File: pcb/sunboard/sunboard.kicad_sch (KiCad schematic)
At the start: 198 parts, among them SW1 SW_Push_LED, SW10 SW_Push_LED, SW100 SW_Push_LED, SW101 SW_Push_LED, SW102 SW_Push_LED, SW103 SW_Push_LED, SW104 SW_Push_LED, SW105 SW_Push_LED, SW106 SW_Push_LED, SW107 SW_Push_LED, SW108 SW_Push_LED, SW109 SW_Push_LED, SW11 SW_Push_LED, SW110 SW_Push_LED, SW111 SW_Push_LED, SW112 SW_Push_LED, SW113 SW_Push_LED, SW114 SW_Push_LED, SW115 SW_Push_LED, SW116 SW_Push_LED, SW117 SW_Push_LED, SW118 SW_Push_LED, SW119 SW_Push_LED, SW12 SW_Push_LED, SW120 SW_Push_LED, SW121 SW_Push_LED, SW122 SW_Push_LED, SW123 SW_Push_LED, SW124 SW_Push_LED, SW125 SW_Push_LED, SW126 SW_Push_LED, SW127 SW_Push_LED, SW128 SW_Push_LED, SW129 SW_Push_LED, SW13 SW_Push_LED, SW130 SW_Push_LED, SW131 SW_Push_LED, SW132 SW_Push_LED, SW133 SW_Push_LED, SW134 SW_Push_LED, SW135 SW_Push_LED, SW136 SW_Push_LED, SW137 SW_Push_LED, SW138 SW_Push_LED, SW139 SW_Push_LED, SW14 SW_Push_LED, SW140 SW_Push_LED, SW141 SW_Push_LED, SW142 SW_Push_LED, SW143 SW_Push_LED, SW144 SW_Push_LED, SW145 SW_Push_LED, SW146 SW_Push_LED, SW147 SW_Push_LED, SW148 SW_Push_LED, SW149 SW_Push_LED, SW15 SW_Push_LED, SW150 SW_Push_LED, SW151 SW_Push_LED, SW152 SW_Push_LED, SW153 SW_Push_LED, SW154 SW_Push_LED, SW155 SW_Push_LED, SW156 SW_Push_LED, SW157 SW_Push_LED, SW158 SW_Push_LED, SW159 SW_Push_LED, SW16 SW_Push_LED, SW160 SW_Push_LED, SW161 SW_Push_LED, SW162 SW_Push_LED, SW163 SW_Push_LED, SW164 SW_Push_LED, SW165 SW_Push_LED, SW166 SW_Push_LED, SW167 SW_Push_LED, SW168 SW_Push_LED, SW169 SW_Push_LED, SW17 SW_Push_LED, SW170 SW_Push_LED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

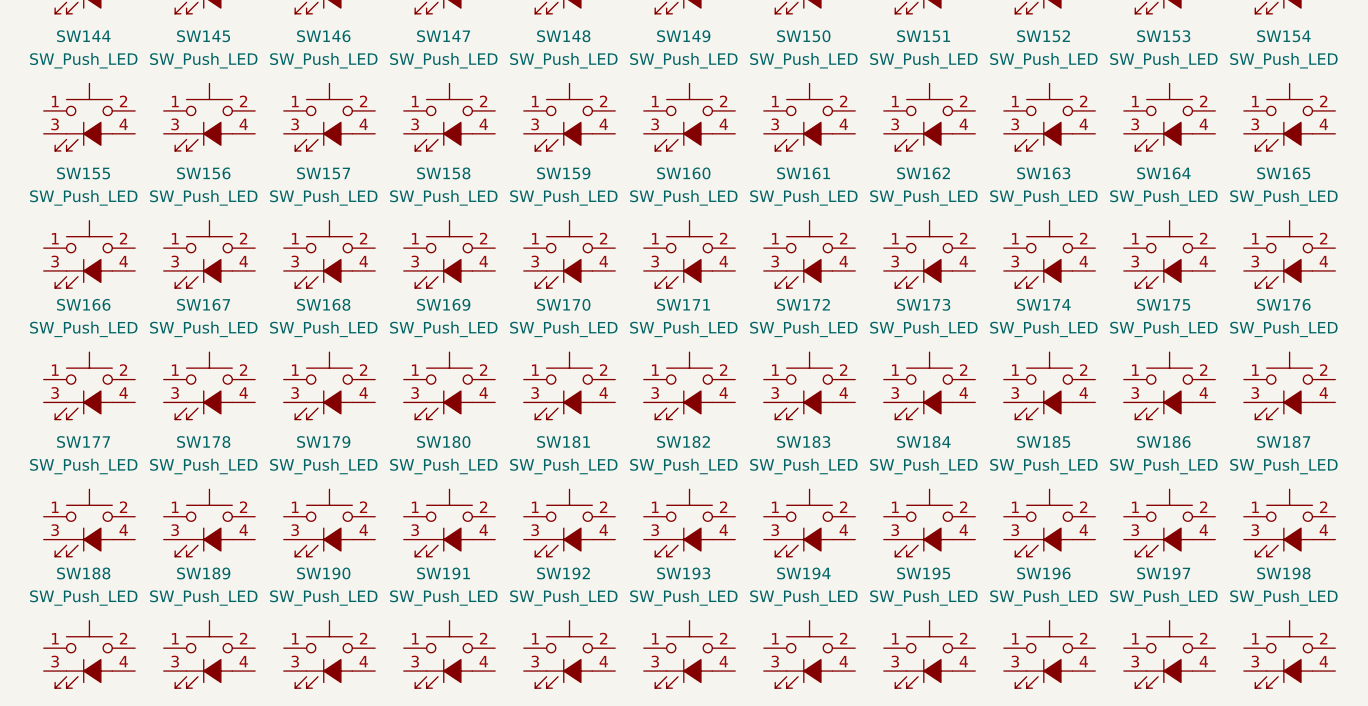
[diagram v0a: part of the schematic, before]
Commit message: feat: remove bottom 4 rows of buttons (footholds)
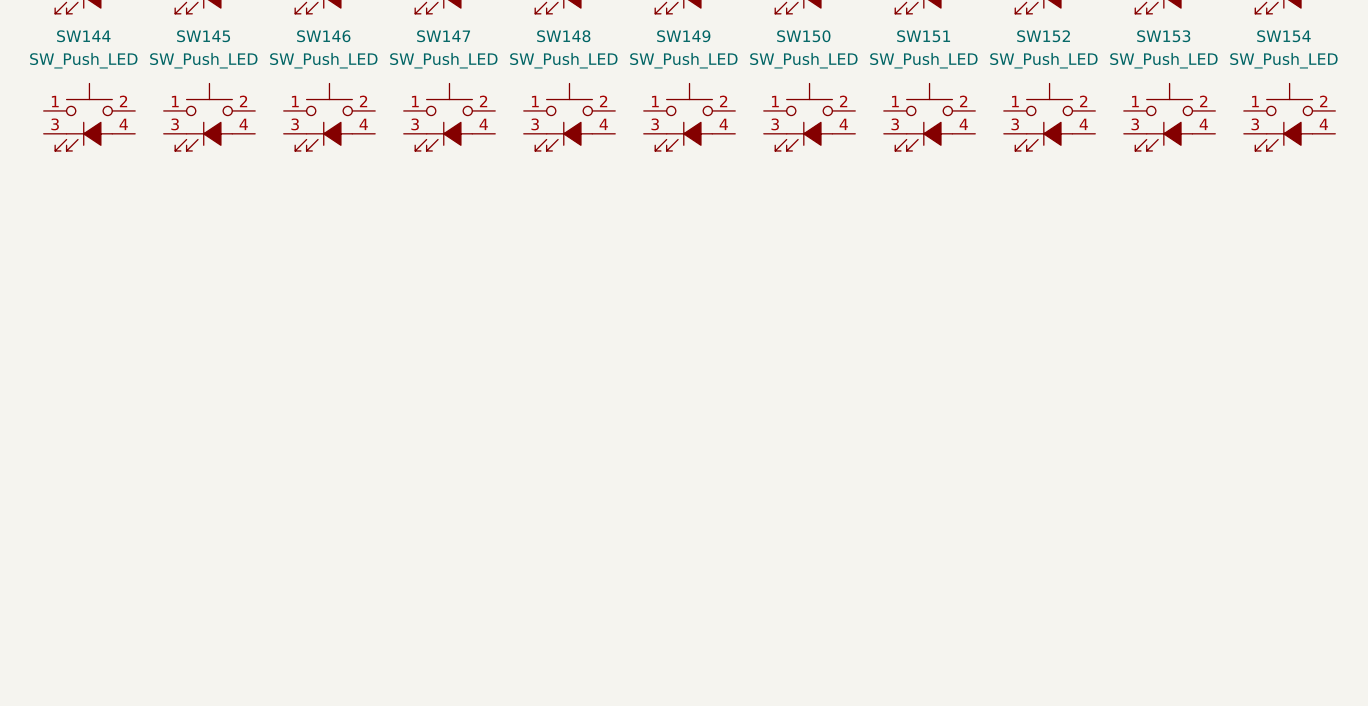
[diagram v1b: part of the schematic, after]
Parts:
- removed SW155, SW156, SW157, SW158, SW159, SW160, SW161, SW162, SW163, SW164, SW165, SW166, SW167, SW168, SW169, SW170, SW171, SW172, SW173, SW174, SW175, SW176, SW177, SW178, SW179, SW180, SW181, SW182, SW183, SW184, SW185, SW186, SW187, SW188, SW189, SW190, SW191, SW192, SW193, SW194, SW195, SW196, SW197, SW198: SW_Push_LED, symbol Switch:SW_Push_LED

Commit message: feat: get basic POC for 8x8 out
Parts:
- removed SW10, SW100, SW101, SW102, SW103, SW104, SW105, SW106, SW107, SW108, SW109, SW11, SW110, SW111, SW112, SW113, SW114, SW115, SW116, SW117, SW118, SW119, SW120, SW121, SW122, SW123, SW124, SW125, SW126, SW127, SW128, SW129, SW130, SW131, SW132, SW133, SW134, SW135, SW136, SW137, SW138, SW139, SW140, SW141, SW142, SW143, SW144, SW145, SW146, SW147, SW148, SW149, SW150, SW151, SW152, SW153, SW154, SW20, SW21, SW22, SW31, SW32, SW33, SW42, SW43, SW44, SW53, SW54, SW55, SW64, SW65, SW66, SW75, SW76, SW77, SW86, SW87, SW88, SW89, SW9, SW90, SW91, SW92, SW93, SW94, SW95, SW96, SW97, SW98, SW99: SW_Push_LED, symbol Switch:SW_Push_LED
- added A?: Adafruit_Feather_HUZZAH32_ESP32, Module:Adafruit_Feather, symbol MCU_Module:Adafruit_Feather_HUZZAH32_ESP32
- added U?: 74LS148, symbol 74xx:74LS148
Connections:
- net at SW74.2: now also SW19.2, SW19.4 (A), SW30.2, SW30.4 (A), SW41.2, SW41.4 (A), SW52.2, SW52.4 (A), SW63.2, SW63.4 (A), SW74.4 (A), SW8.2, SW8.4 (A), SW85.2, U?.11 (I1)
- net at SW70.2: now also SW15.2, SW15.4 (A), SW26.2, SW26.4 (A), SW37.2, SW37.4 (A), SW4.2, SW4.4 (A), SW48.2, SW48.4 (A), SW59.2, SW59.4 (A), SW70.4 (A), SW81.2, U?.2 (I5)
- net at SW72.2: now also SW17.2, SW17.4 (A), SW28.2, SW28.4 (A), SW39.2, SW39.4 (A), SW50.2, SW50.4 (A), SW6.2, SW6.4 (A), SW61.2, SW61.4 (A), SW72.4 (A), SW83.2, U?.13 (I3)
- net at SW24.2: now also SW13.2, SW13.4 (A), SW2.2, SW2.4 (A), SW24.4 (A), SW35.2, SW35.4 (A), SW46.2, SW46.4 (A), SW57.2, SW57.4 (A), SW68.2, SW68.4 (A), SW79.2, U?.4 (I7)
- net at SW45.2: now also SW1.2, SW1.4 (A), SW12.2, SW23.2, SW23.4 (A), SW34.2, SW34.4 (A), SW45.4 (A), SW56.2, SW56.4 (A), SW67.2, SW67.4 (A), SW78.2, U?.5 (EI)
- net at SW62.2: now also SW18.2, SW18.4 (A), SW29.2, SW29.4 (A), SW40.2, SW40.4 (A), SW51.2, SW51.4 (A), SW62.4 (A), SW7.2, SW7.4 (A), SW73.2, SW73.4 (A), SW84.2, U?.12 (I2)
- net at SW25.2: now also SW14.2, SW14.4 (A), SW25.4 (A), SW3.2, SW3.4 (A), SW36.2, SW36.4 (A), SW47.2, SW47.4 (A), SW58.2, SW58.4 (A), SW69.2, SW69.4 (A), SW80.2, U?.3 (I6)
- net at SW60.2: now also SW16.2, SW16.4 (A), SW27.2, SW27.4 (A), SW38.2, SW38.4 (A), SW49.2, SW49.4 (A), SW5.2, SW5.4 (A), SW60.4 (A), SW71.2, SW71.4 (A), SW82.2, U?.1 (I4)
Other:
- moved on the sheet: SW1, SW12, SW13, SW14, SW15, SW16, SW17, SW18, SW19, SW2, SW23, SW24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

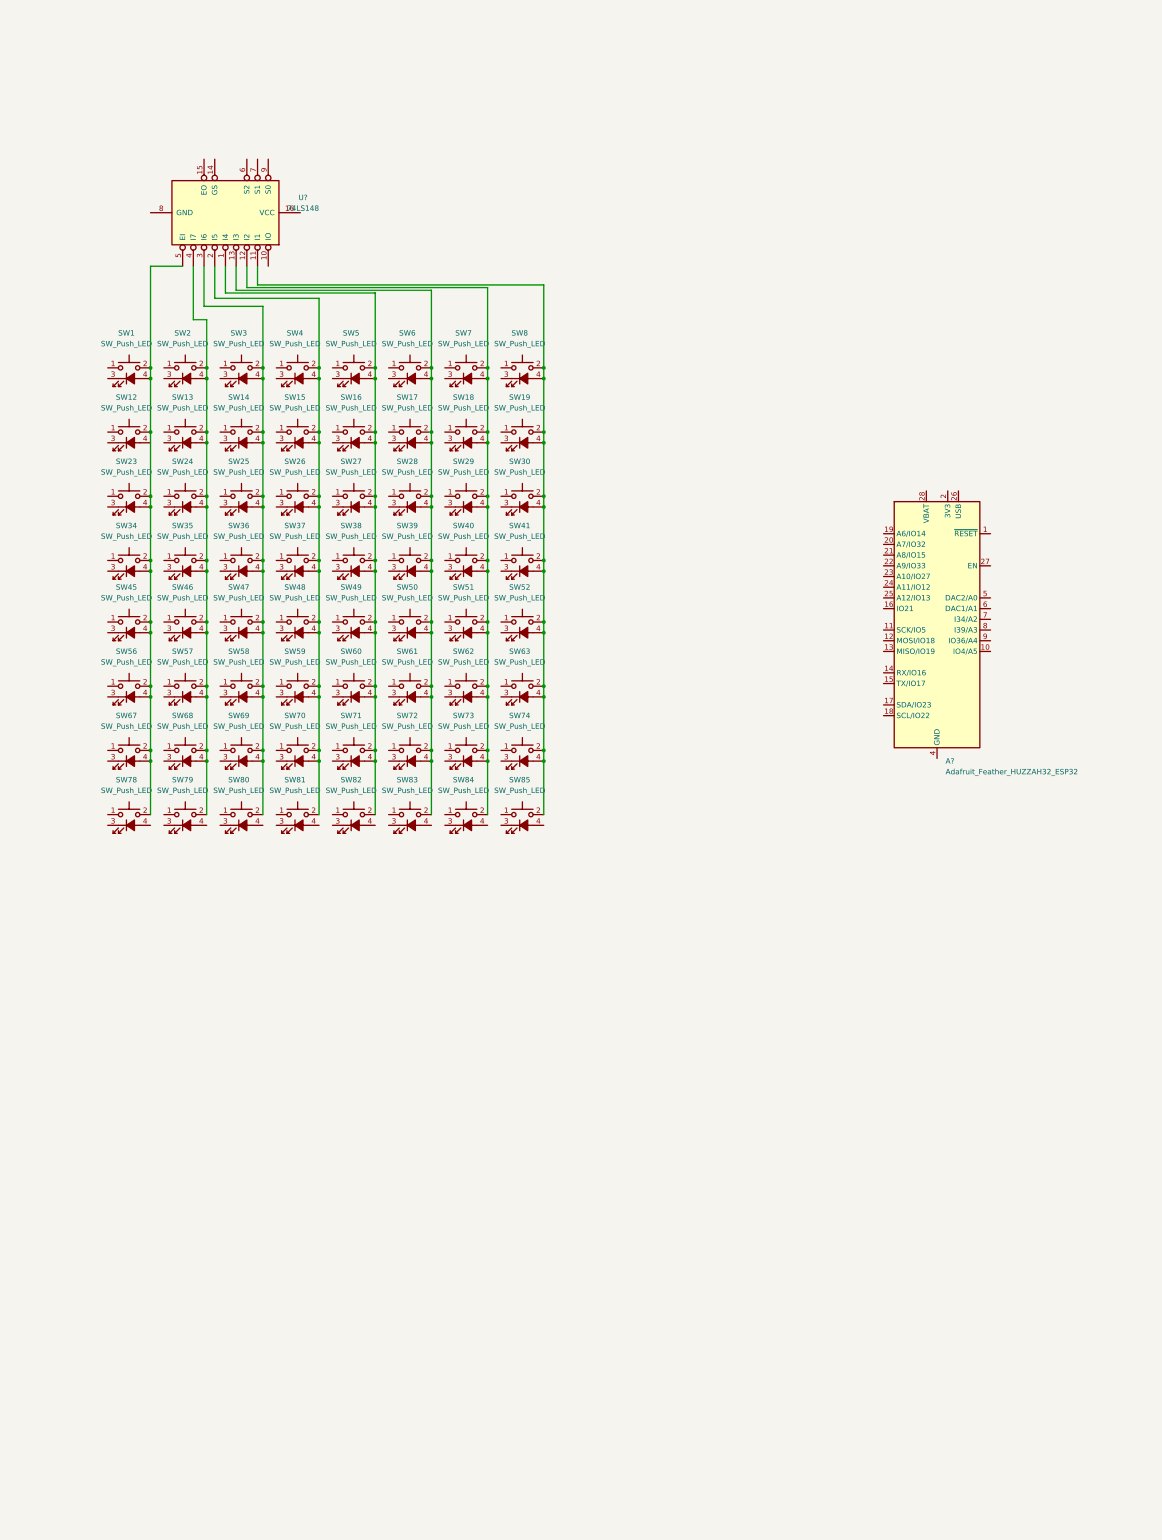
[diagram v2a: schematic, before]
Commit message: feat(pcb): add nets for rows and columns
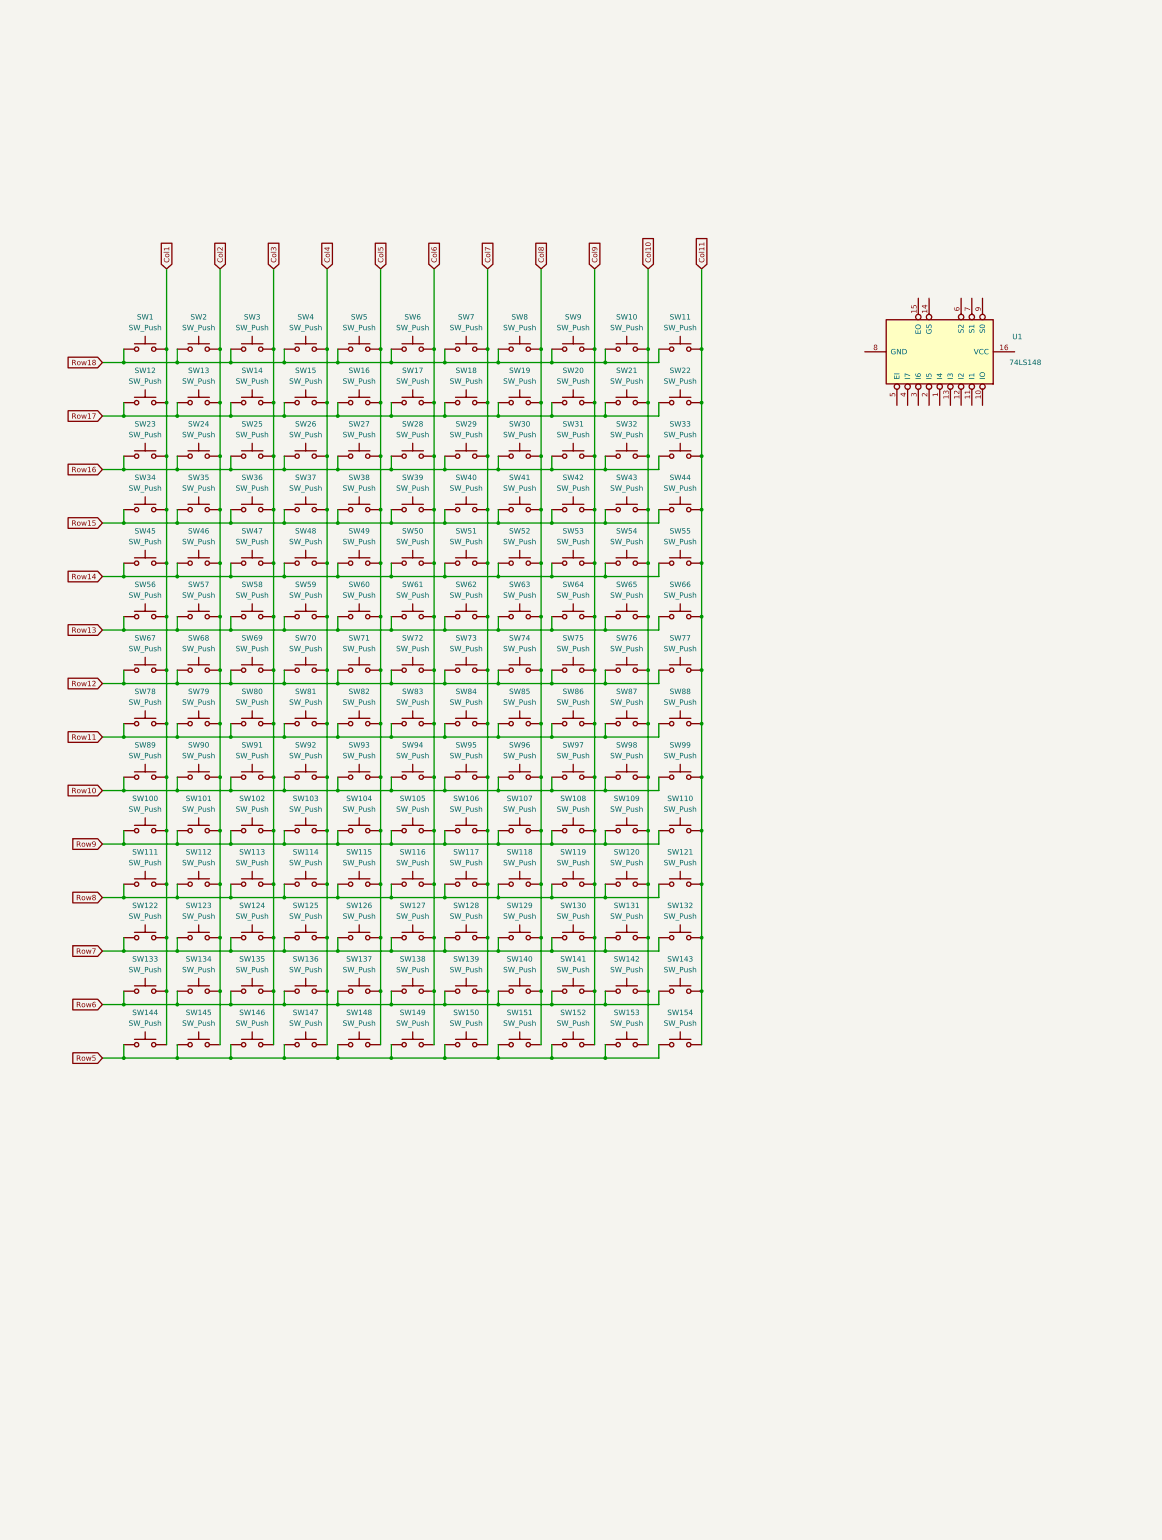
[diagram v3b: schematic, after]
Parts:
- removed A?: Adafruit_Feather_HUZZAH32_ESP32, Module:Adafruit_Feather, symbol MCU_Module:Adafruit_Feather_HUZZAH32_ESP32
- removed SW1, SW12, SW13, SW14, SW15, SW16, SW17, SW18, SW19, SW2, SW23, SW24, SW25, SW26, SW27, SW28, SW29, SW3, SW30, SW34, SW35, SW36, SW37, SW38, SW39, SW4, SW40, SW41, SW45, SW46, SW47, SW48, SW49, SW5, SW50, SW51, SW52, SW56, SW57, SW58, SW59, SW6, SW60, SW61, SW62, SW63, SW67, SW68, SW69, SW7, SW70, SW71, SW72, SW73, SW74, SW78, SW79, SW8, SW80, SW81, SW82, SW83, SW84, SW85: SW_Push_LED, symbol Switch:SW_Push_LED
- added SW1, SW10, SW100, SW101, SW102, SW103, SW104, SW105, SW106, SW107, SW108, SW109, SW11, SW110, SW111, SW112, SW113, SW114, SW115, SW116, SW117, SW118, SW119, SW12, SW120, SW121, SW122, SW123, SW124, SW125, SW126, SW127, SW128, SW129, SW13, SW130, SW131, SW132, SW133, SW134, SW135, SW136, SW137, SW138, SW139, SW14, SW140, SW141, SW142, SW143, SW144, SW145, SW146, SW147, SW148, SW149, SW15, SW150, SW151, SW152, SW153, SW154, SW16, SW17, SW18, SW19, SW2, SW20, SW21, SW22, SW23, SW24, SW25, SW26, SW27, SW28, SW29, SW3, SW30, SW31, SW32, SW33, SW34, SW35, SW36, SW37, SW38, SW39, SW4, SW40, SW41, SW42, SW43, SW44, SW45, SW46, SW47, SW48, SW49, SW5, SW50, SW51, SW52, SW53, SW54, SW55, SW56, SW57, SW58, SW59, SW6, SW60, SW61, SW62, SW63, SW64, SW65, SW66, SW67, SW68, SW69, SW7, SW70, SW71, SW72, SW73, SW74, SW75, SW76, SW77, SW78, SW79, SW8, SW80, SW81, SW82, SW83, SW84, SW85, SW86, SW87, SW88, SW89, SW9, SW90, SW91, SW92, SW93, SW94, SW95, SW96, SW97, SW98, SW99: SW_Push, symbol Switch:SW_Push
- gave numbers to parts that had none: 1
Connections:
- new net Col1: SW1.2, SW100.2, SW111.2, SW12.2, SW122.2, SW133.2, SW144.2, SW23.2, SW34.2, SW45.2, SW56.2, SW67.2, SW78.2, SW89.2
- new net Col10: SW10.2, SW109.2, SW120.2, SW131.2, SW142.2, SW153.2, SW21.2, SW32.2, SW43.2, SW54.2, SW65.2, SW76.2, SW87.2, SW98.2
- new net Col11: SW11.2, SW110.2, SW121.2, SW132.2, SW143.2, SW154.2, SW22.2, SW33.2, SW44.2, SW55.2, SW66.2, SW77.2, SW88.2, SW99.2
- new net Col2: SW101.2, SW112.2, SW123.2, SW13.2, SW134.2, SW145.2, SW2.2, SW24.2, SW35.2, SW46.2, SW57.2, SW68.2, SW79.2, SW90.2
- new net Col3: SW102.2, SW113.2, SW124.2, SW135.2, SW14.2, SW146.2, SW25.2, SW3.2, SW36.2, SW47.2, SW58.2, SW69.2, SW80.2, SW91.2
- new net Col4: SW103.2, SW114.2, SW125.2, SW136.2, SW147.2, SW15.2, SW26.2, SW37.2, SW4.2, SW48.2, SW59.2, SW70.2, SW81.2, SW92.2
- new net Col5: SW104.2, SW115.2, SW126.2, SW137.2, SW148.2, SW16.2, SW27.2, SW38.2, SW49.2, SW5.2, SW60.2, SW71.2, SW82.2, SW93.2
- new net Col6: SW105.2, SW116.2, SW127.2, SW138.2, SW149.2, SW17.2, SW28.2, SW39.2, SW50.2, SW6.2, SW61.2, SW72.2, SW83.2, SW94.2
- new net Col7: SW106.2, SW117.2, SW128.2, SW139.2, SW150.2, SW18.2, SW29.2, SW40.2, SW51.2, SW62.2, SW7.2, SW73.2, SW84.2, SW95.2
- new net Col8: SW107.2, SW118.2, SW129.2, SW140.2, SW151.2, SW19.2, SW30.2, SW41.2, SW52.2, SW63.2, SW74.2, SW8.2, SW85.2, SW96.2
- new net Col9: SW108.2, SW119.2, SW130.2, SW141.2, SW152.2, SW20.2, SW31.2, SW42.2, SW53.2, SW64.2, SW75.2, SW86.2, SW9.2, SW97.2
- new net Row10: SW89.1, SW90.1, SW91.1, SW92.1, SW93.1, SW94.1, SW95.1, SW96.1, SW97.1, SW98.1, SW99.1
- new net Row11: SW78.1, SW79.1, SW80.1, SW81.1, SW82.1, SW83.1, SW84.1, SW85.1, SW86.1, SW87.1, SW88.1
- new net Row12: SW67.1, SW68.1, SW69.1, SW70.1, SW71.1, SW72.1, SW73.1, SW74.1, SW75.1, SW76.1, SW77.1
- new net Row13: SW56.1, SW57.1, SW58.1, SW59.1, SW60.1, SW61.1, SW62.1, SW63.1, SW64.1, SW65.1, SW66.1
- new net Row14: SW45.1, SW46.1, SW47.1, SW48.1, SW49.1, SW50.1, SW51.1, SW52.1, SW53.1, SW54.1, SW55.1
- new net Row15: SW34.1, SW35.1, SW36.1, SW37.1, SW38.1, SW39.1, SW40.1, SW41.1, SW42.1, SW43.1, SW44.1
- new net Row16: SW23.1, SW24.1, SW25.1, SW26.1, SW27.1, SW28.1, SW29.1, SW30.1, SW31.1, SW32.1, SW33.1
- new net Row17: SW12.1, SW13.1, SW14.1, SW15.1, SW16.1, SW17.1, SW18.1, SW19.1, SW20.1, SW21.1, SW22.1
- new net Row18: SW1.1, SW10.1, SW11.1, SW2.1, SW3.1, SW4.1, SW5.1, SW6.1, SW7.1, SW8.1, SW9.1
- new net Row5: SW144.1, SW145.1, SW146.1, SW147.1, SW148.1, SW149.1, SW150.1, SW151.1, SW152.1, SW153.1, SW154.1
- new net Row6: SW133.1, SW134.1, SW135.1, SW136.1, SW137.1, SW138.1, SW139.1, SW140.1, SW141.1, SW142.1, SW143.1
- new net Row7: SW122.1, SW123.1, SW124.1, SW125.1, SW126.1, SW127.1, SW128.1, SW129.1, SW130.1, SW131.1, SW132.1
- new net Row8: SW111.1, SW112.1, SW113.1, SW114.1, SW115.1, SW116.1, SW117.1, SW118.1, SW119.1, SW120.1, SW121.1
- new net Row9: SW100.1, SW101.1, SW102.1, SW103.1, SW104.1, SW105.1, SW106.1, SW107.1, SW108.1, SW109.1, SW110.1
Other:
- moved on the sheet: U1
